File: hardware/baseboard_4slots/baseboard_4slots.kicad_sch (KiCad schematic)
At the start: 37 parts

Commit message: More files cleaned up + Some work on baseboard
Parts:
- C1, C2, C3, C4, C5, C6, C7, C8: value (none) -> 100nF; footprint (none) -> Capacitor_SMD:C_0603_1608Metric
- C10, C11, C12, C13, C9: value (none) -> 1nF; footprint (none) -> Capacitor_SMD:C_0603_1608Metric
- D1: value (none) -> SS14; footprint (none) -> Diode_SMD:D_SMA
- H1, H10, H2, H3, H4, H5, H6, H7, H8, H9: value (none) -> MountingHole; footprint (none) -> MountingHole:MountingHole_3.2mm_M3
- J1: value (none) -> IO-Board_00; footprint (none) -> Connector_PinSocket_2.54mm:PinSocket_2x06_P2.54mm_Vertical
- J2: value (none) -> IO-Board_01; footprint (none) -> Connector_PinSocket_2.54mm:PinSocket_2x06_P2.54mm_Vertical
- J3: value (none) -> IO-Board_10; footprint (none) -> Connector_PinSocket_2.54mm:PinSocket_2x06_P2.54mm_Vertical
- J4: value (none) -> IO-Board_11; footprint (none) -> Connector_PinSocket_2.54mm:PinSocket_2x06_P2.54mm_Vertical
- J5: value (none) -> USB_B_Micro; footprint (none) -> Connector_USB:USB_Micro-B_Wuerth_629105150521
- J6: value (none) -> Conn_01x05: Adafruit 1833; footprint (none) -> Connector_PinHeader_2.54mm:PinHeader_1x05_P2.54mm_Vertical
- J7: value (none) -> Screw_Terminal_01x04; footprint (none) -> TerminalBlock:TerminalBlock_Altech_AK300-4_P5.00mm
- J8, J9: value (none) -> Conn_02x02_Odd_Even; footprint (none) -> Connector_PinHeader_2.54mm:PinHeader_2x02_P2.54mm_Vertical
- R1, R2: value (none) -> 2k; footprint (none) -> Resistor_SMD:R_0805_2012Metric_Pad1.20x1.40mm_HandSolder
- U1: value (none) -> NRF24L01_Breakout; footprint (none) -> RF_Module:nRF24L01_Breakout
- U2: value (none) -> Pico; footprint (none) -> MCU_RaspberryPi_and_Boards:RPi_Pico_SMD_TH

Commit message: Some more work on the baseboard
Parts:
- added C14, C15, C16, C17, C18, C19, C20, C25, C26: 82µF, Capacitor_THT:CP_Radial_D6.3mm_P2.50mm, symbol Device:C_Polarized
- added C21, C22, C27, C28: 100nF, Capacitor_SMD:C_0603_1608Metric, symbol Device:C
- added C23, C24, C29, C30: 1nF, Capacitor_SMD:C_0603_1608Metric, symbol Device:C
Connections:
- net GND: now also C14.2, C15.2, C16.2, C17.2, C18.2, C19.2, C20.2, C21.2, C22.2, C23.2, C24.2, C25.2, C26.2, C27.2, C28.2, C29.2, C30.2
- net VDD: now also C15.1, C16.1, C17.1, C18.1
- net +3V3 renamed +3.3V
- net +3.3V: now also C14.1, C19.1, C20.1, C21.1, C22.1, C23.1, C24.1, C25.1, C26.1, C27.1, C28.1, C29.1, C30.1
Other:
- moved on the sheet: C1, C10, C11, C12, C13, C4, C5, C6, C7, C9, J1, J2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

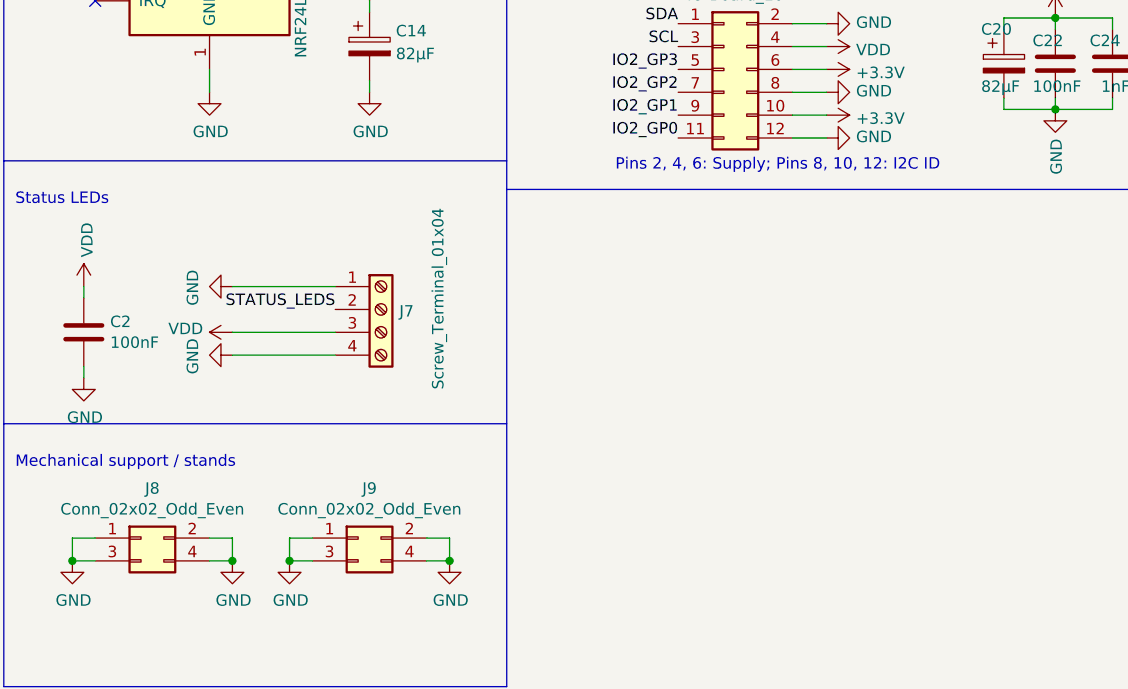
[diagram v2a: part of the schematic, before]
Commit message: Add I2C expansion connectors and a Grove connector for the status LEDs
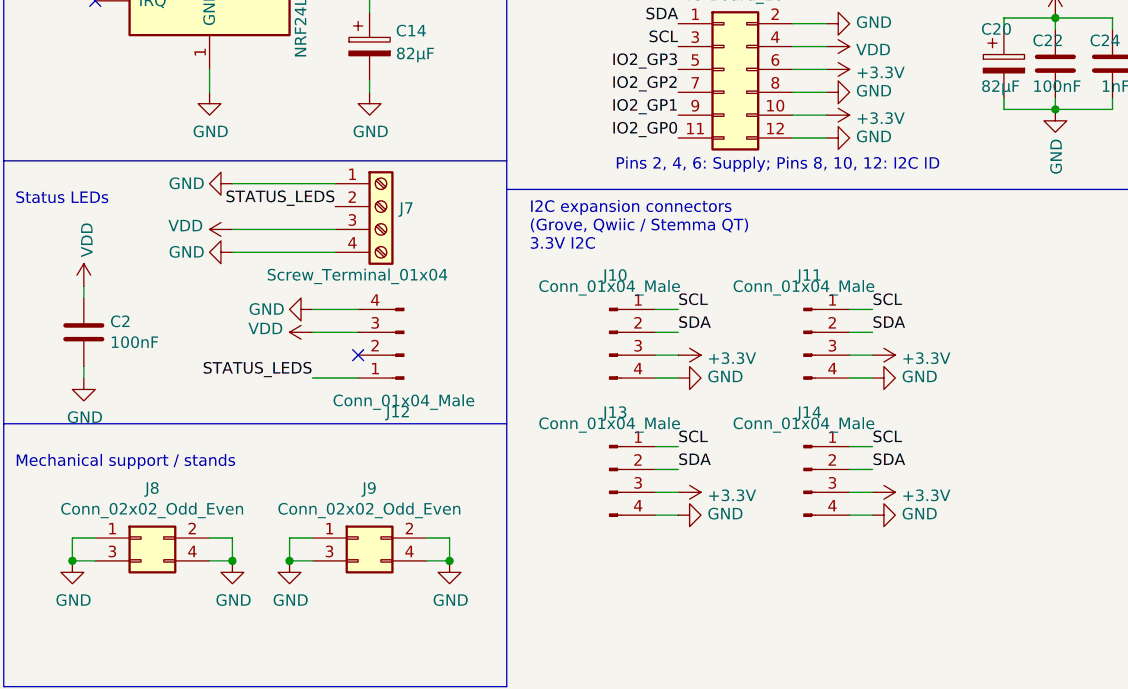
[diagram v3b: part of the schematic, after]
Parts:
- added J10, J11, J12: Conn_01x04_Male, Connector:NS-Tech_Grove_1x04_P2mm_Vertical, symbol Connector:Conn_01x04_Male
- added J13, J14: Conn_01x04_Male, Connector_JST:JST_SH_BM04B-SRSS-TB_1x04-1MP_P1.00mm_Vertical, symbol Connector:Conn_01x04_Male
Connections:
- net +3.3V: now also J10.3 (Pin_3), J11.3 (Pin_3), J13.3 (Pin_3), J14.3 (Pin_3)
- net GND: now also J10.4 (Pin_4), J11.4 (Pin_4), J12.4 (Pin_4), J13.4 (Pin_4), J14.4 (Pin_4)
- net SCL: now also J10.1 (Pin_1), J11.1 (Pin_1), J13.1 (Pin_1), J14.1 (Pin_1)
- net SDA: now also J10.2 (Pin_2), J11.2 (Pin_2), J13.2 (Pin_2), J14.2 (Pin_2)
- net STATUS_LEDS: now also J12.1 (Pin_1)
- net VDD: now also J12.3 (Pin_3)
- no-connect marks 16 -> 17
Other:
- note added: "I2C expansion connectors (Grove, Qwiic / Stemma QT) 3.3V I2C"
- moved on the sheet: J7
